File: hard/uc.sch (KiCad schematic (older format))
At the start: 31 parts, among them J3 Conn_01x06, M97 2N7002,215

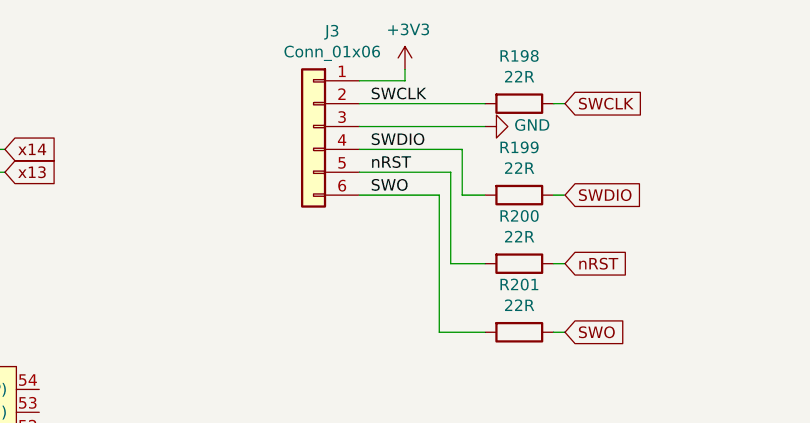
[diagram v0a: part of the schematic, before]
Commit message: added led driver layout by @lukekaese
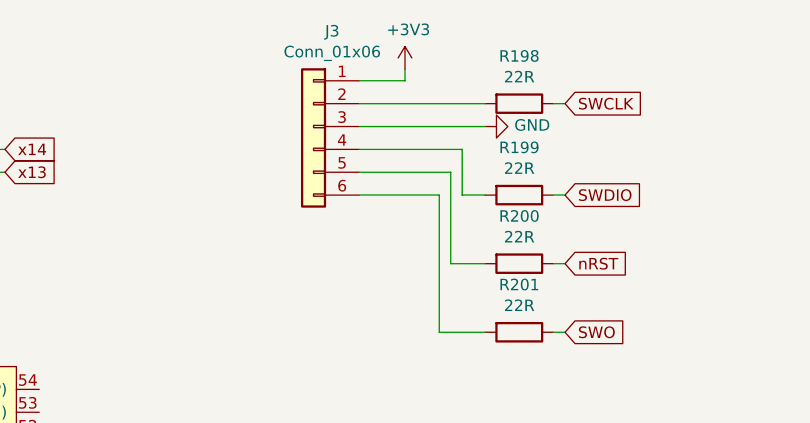
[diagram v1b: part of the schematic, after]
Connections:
- net SWCLK: no longer J3.2 (Pin_2), R198.2
- net SWDIO: no longer J3.4 (Pin_4), R199.2
- net SWO: no longer J3.6 (Pin_6), R201.2
- net nRST: no longer J3.5 (Pin_5), R200.2
- new net: J3.5 (Pin_5), R200.2
- new net: J3.4 (Pin_4), R199.2
- new net: J3.2 (Pin_2), R198.2
- new net: J3.6 (Pin_6), R201.2
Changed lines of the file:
@@
 Text GLabel 9950 5700 2    50   Input ~ 0
 y13
-Text Label 13100 1900 0    50   ~ 0
-SWCLK
-Text Label 13100 2100 0    50   ~ 0
-SWDIO
-Text Label 13100 2200 0    50   ~ 0
-nRST
-Text Label 13100 2300 0    50   ~ 0
-SWO
 Wire Wire Line
 	13050 1900 13600 1900

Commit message: pcb format refactor
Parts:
- J1: renamed from J3; footprint Connector_PinHeader_2.54mm:PinHeader_1x06_P2.54mm_Horizontal -> Connector_PinHeader_2.54mm:PinHeader_1x06_P2.54mm_Vertical
- renumbered C26 to C12, C27 to C13, C12 to C14, C13 to C15, C14 to C16, C5 to C2, C2 to C3, C3 to C4, C4 to C5, D1028 to D1, M97 to M1, R198 to R1, R207 to R10, R199 to R2, R200 to R3, R201 to R4, R204 to R5, R205 to R6, R202 to R7, R203 to R8, R206 to R9

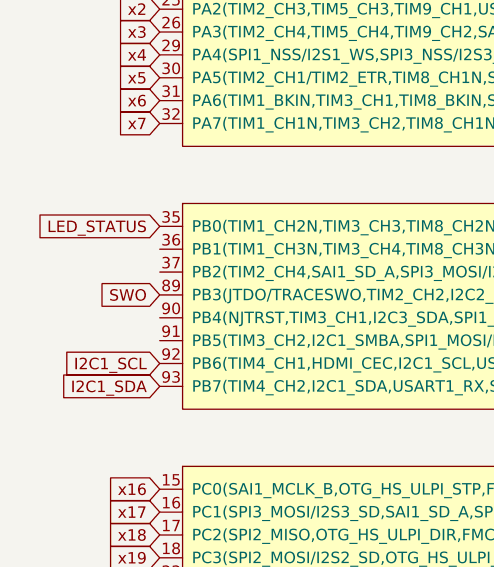
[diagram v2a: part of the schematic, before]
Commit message: general layout update
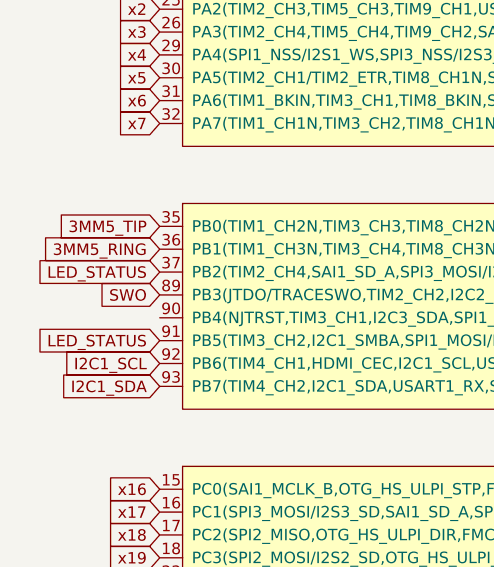
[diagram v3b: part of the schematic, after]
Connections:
- net LED_STATUS: now also MCU1.37 (PB2(TIM2_CH4,SAI1_SD_A,SPI3_MOSI/I2S3_SD,QUADSPI_CLK,OTG_HS_ULPI_D4,SDIO_CK,BOOT1)), MCU1.91 (PB5(TIM3_CH2,I2C1_SMBA,SPI1_MOSI/I2S1_SD,SPI3_MOSI/I2S3_SD,CAN2_RX,OTG_HS_ULPI_D7,FMC_SDCKE1,DCMI_D10)); no longer MCU1.35 (PB0(TIM1_CH2N,TIM3_CH3,TIM8_CH2N,SPI3_MOSI/I2S3_SD,UART4_CTS,OTG_HS_ULPI_D1,SDIO_D1,ADC12_IN8))
- net 3MM5_RING: now reaches MCU1.36 (PB1(TIM1_CH3N,TIM3_CH4,TIM8_CH3N,OTG_HS_ULPI_D2,SDIO_D2,ADC12_IN9))
- new net 3MM5_TIP: MCU1.35 (PB0(TIM1_CH2N,TIM3_CH3,TIM8_CH2N,SPI3_MOSI/I2S3_SD,UART4_CTS,OTG_HS_ULPI_D1,SDIO_D1,ADC12_IN8))
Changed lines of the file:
@@
 Wire Wire Line
 	15950 7500 15950 7550
-Text GLabel 3550 3150 0    50   Input ~ 0
+Text GLabel 3550 3350 0    50   Input ~ 0
 LED_STATUS
 Wire Wire Line
@@
 Wire Wire Line
 	15350 5000 15400 5000
+Text GLabel 3550 3150 0    50   Input ~ 0
+3MM5_TIP
+Text GLabel 3550 3250 0    50   Input ~ 0
+3MM5_RING
+Text GLabel 3550 3650 0    50   Input ~ 0
+LED_STATUS
 $EndSCHEMATC

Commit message: layout process
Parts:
- removed unit 6 of MCU1
- removed R5, R6: 3K3, Resistor_SMD:R_0402_1005Metric, symbol Device:R
- J1: footprint Connector_PinHeader_2.54mm:PinHeader_1x06_P2.54mm_Vertical -> Connector_PinHeader_2.54mm:PinHeader_1x06_P2.54mm_Horizontal
- MCU1: footprint (none) -> Package_QFP:LQFP-100_14x14mm_P0.5mm
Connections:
- net y16: no longer MCU1.97 (PE0(TIM4_ETR,SAI2_MCLK_A,FMC_NBL0,DCMI_D2))
- net y17: no longer MCU1.98 (PE1(FMC_NBL1,DCMI_D3))
- net SPI2_CS_ACC: now reaches MCU1.51 (PB12(TIM1_BKIN,I2C2_SMBA,SPI2_NSS/I2S2_WS,SAI1_SCK_B,USART3_CK,CAN2_RX,OTG_HS_ULPI_D5,OTG_HS_ID))
- net SPI2_SCLK: now reaches MCU1.52 (PB13(TIM1_CH1N,SPI2_SCK/I2S2_CK,USART3_CTS,CAN2_TX,OTG_HS_ULPI_D6,OTG_HS_VBUS))
- net SPI2_MISO: now reaches MCU1.53 (PB14(TIM1_CH2N,TIM8_CH2N,SPI2_MISO,USART3_RTS,TIM12_CH1,OTG_HS_DM))
- net SPI2_MOSI: now reaches MCU1.54 (PB15(RTC_REFIN,TIM1_CH3N,TIM8_CH3N,SPI2_MOSI/I2S2_SD,TIM12_CH2,OTG_HS_DP))
- net SWCLK renamed x14
- net SWDIO renamed x13
- new net ACC_INT1: MCU1.97 (PE0(TIM4_ETR,SAI2_MCLK_A,FMC_NBL0,DCMI_D2))
- new net ACC_INT2: MCU1.98 (PE1(FMC_NBL1,DCMI_D3))
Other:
- note added: "+3V3"
- note added: "GND"
- note added: "SWCLK"
- note added: "SWDIO"
- note added: "SWO"
- note added: "nRST"
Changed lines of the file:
@@
 F 0 "MCU1" H 7300 2065 50  0000 C CNN
 F 1 "STM32F446VE" H 7300 1974 50  0000 C CNN
-F 2 "" H 7850 2250 50  0001 C CNN
+F 2 "Package_QFP:LQFP-100_14x14mm_P0.5mm" H 7850 2250 50  0001 C CNN
 F 3 "https://www.st.com/resource/en/datasheet/stm32f446ve.pdf" H 7850 2250 50  0001 C CNN
 F 4 "C91929" H 7300 1900 50  0001 C CNN "JLCPCB_Part_Number"
@@
 F 0 "MCU1" H 7600 3215 50  0000 C CNN
 F 1 "STM32F446VE" H 7600 3124 50  0000 C CNN
-F 2 "" H 8150 3400 50  0001 C CNN
+F 2 "Package_QFP:LQFP-100_14x14mm_P0.5mm" H 8150 3400 50  0001 C CNN
 F 3 "https://www.st.com/resource/en/datasheet/stm32f446ve.pdf" H 8150 3400 50  0001 C CNN
 F 4 "C91929" H 7600 3050 50  0001 C CNN "JLCPCB_Part_Number"
@@
 F 0 "MCU1" H 7700 4365 50  0000 C CNN
 F 1 "STM32F446VE" H 7700 4274 50  0000 C CNN
-F 2 "" H 8250 4550 50  0001 C CNN
+F 2 "Package_QFP:LQFP-100_14x14mm_P0.5mm" H 8250 4550 50  0001 C CNN
 F 3 "https://www.st.com/resource/en/datasheet/stm32f446ve.pdf" H 8250 4550 50  0001 C CNN
 F 4 "C91929" H 7700 4200 50  0001 C CNN "JLCPCB_Part_Number"
@@
 $Comp
 L led_matrix:STM32F446VE MCU1
-U 6 1 605B418A
-P 4250 7800
-F 0 "MCU1" H 4250 7965 50  0000 C CNN
-F 1 "STM32F446VE" H 4250 7874 50  0000 C CNN
-F 2 "" H 4800 8150 50  0001 C CNN
-F 3 "https://www.st.com/resource/en/datasheet/stm32f446ve.pdf" H 4800 8150 50  0001 C CNN
-F 4 "C91929" H 4250 7800 50  0001 C CNN "JLCPCB_Part_Number"
-F 5 "STMicroelectronics" H 4250 7800 50  0001 C CNN "MF"
-F 6 "STM32F446VET6" H 4250 7800 50  0001 C CNN "MPN"
-F 7 "ST MICROELECTRONICS LQFP-100_14X14X05P ROHS" H 4250 7800 50  0001 C CNN "Description"
-	6    4250 7800
-	1    0    0    -1
-$EndComp
-$Comp
-L led_matrix:STM32F446VE MCU1
 U 7 1 605B81AB
 P 12900 6100
 F 0 "MCU1" H 12900 6265 50  0000 C CNN
 F 1 "STM32F446VE" H 12900 6174 50  0000 C CNN
-F 2 "" H 13450 6450 50  0001 C CNN
+F 2 "Package_QFP:LQFP-100_14x14mm_P0.5mm" H 13450 6450 50  0001 C CNN
 F 3 "https://www.st.com/resource/en/datasheet/stm32f446ve.pdf" H 13450 6450 50  0001 C CNN
 F 4 "C91929" H 12900 6100 50  0001 C CNN "JLCPCB_Part_Number"
@@
 	11200 6200 11250 6200
 Text GLabel 13950 1900 2    50   Input ~ 0
-SWCLK
+x14
 Text GLabel 13950 2300 2    50   Input ~ 0
-SWDIO
+x13
 $Comp
 L power:GND #PWR02
@@
 L power:+3V3 #PWR01
 U 1 1 6266BC9A
-P 13250 1750
-F 0 "#PWR01" H 13250 1600 50  0001 C CNN
-F 1 "+3V3" H 13265 1923 50  0000 C CNN
-F 2 "" H 13250 1750 50  0001 C CNN
-F 3 "" H 13250 1750 50  0001 C CNN
-	1    13250 1750
+P 13600 1750
+F 0 "#PWR01" H 13600 1600 50  0001 C CNN
+F 1 "+3V3" H 13615 1923 50  0000 C CNN
+F 2 "" H 13600 1750 50  0001 C CNN
+F 3 "" H 13600 1750 50  0001 C CNN
+	1    13600 1750
 	1    0    0    -1
 $EndComp
@@
 F 0 "J1" H 12768 2417 50  0000 C CNN
 F 1 "Conn_01x06" H 12768 2326 50  0000 C CNN
-F 2 "Connector_PinHeader_2.54mm:PinHeader_1x06_P2.54mm_Vertical" H 12850 2000 50  0001 C CNN
+F 2 "Connector_PinHeader_2.54mm:PinHeader_1x06_P2.54mm_Horizontal" H 12850 2000 50  0001 C CNN
 F 3 "~" H 12850 2000 50  0001 C CNN
 	1    12850 2000
@@
 SWO
 Wire Wire Line
-	13050 1800 13250 1800
-Wire Wire Line
-	13250 1800 13250 1750
+	13050 1800 13600 1800
+Wire Wire Line
+	13600 1800 13600 1750
 Wire Wire Line
 	13900 2900 13950 2900
@@
 Text GLabel 3550 3850 0    50   Input ~ 0
 I2C1_SDA
-$Comp
-L Device:R R5
-U 1 1 627218B8
-P 15350 5200
-F 0 "R5" H 15281 5154 50  0000 R CNN
-F 1 "3K3" H 15281 5245 50  0000 R CNN
-F 2 "Resistor_SMD:R_0402_1005Metric" V 15280 5200 50  0001 C CNN
-F 3 "~" H 15350 5200 50  0001 C CNN
-	1    15350 5200
-	1    0    0    1
-$EndComp
-$Comp
-L Device:R R6
-U 1 1 62734FB0
-P 15450 5200
-F 0 "R6" H 15380 5154 50  0000 R CNN
-F 1 "3K3" H 15380 5245 50  0000 R CNN
-F 2 "Resistor_SMD:R_0402_1005Metric" V 15380 5200 50  0001 C CNN
-F 3 "~" H 15450 5200 50  0001 C CNN
-	1    15450 5200
-	-1   0    0    1
-$EndComp
-$Comp
-L power:+3V3 #PWR03
-U 1 1 62752189
-P 15400 4950
-F 0 "#PWR03" H 15400 4800 50  0001 C CNN
-F 1 "+3V3" H 15415 5123 50  0000 C CNN
-F 2 "" H 15400 4950 50  0001 C CNN
-F 3 "" H 15400 4950 50  0001 C CNN
-	1    15400 4950
-	1    0    0    -1
-$EndComp
-Text GLabel 15350 5400 3    50   Input ~ 0
-I2C1_SDA
-Text GLabel 15450 5400 3    50   Input ~ 0
-I2C1_SCL
-Wire Wire Line
-	15350 5050 15350 5000
-Wire Wire Line
-	15450 5000 15450 5050
-Wire Wire Line
-	15400 5000 15400 4950
-Connection ~ 15400 5000
-Text Notes 16900 3950 0    50   ~ 0
+Text Notes 12300 4150 0    50   ~ 0
 todo: recheck pins\n
 Text GLabel 3550 2000 0    50   Input ~ 0
@@
 Text GLabel 11050 2300 2    50   Input ~ 0
 x12
-Text GLabel 11500 2200 2    50   Input ~ 0
+Text GLabel 11050 2200 2    50   Input ~ 0
 x13
-Text GLabel 11500 2100 2    50   Input ~ 0
+Text GLabel 11050 2100 2    50   Input ~ 0
 x14
 Text GLabel 11050 2000 2    50   Input ~ 0
@@
 F 0 "MCU1" H 5900 6765 50  0000 C CNN
 F 1 "STM32F446VE" H 5900 6674 50  0000 C CNN
-F 2 "" H 6450 6950 50  0001 C CNN
+F 2 "Package_QFP:LQFP-100_14x14mm_P0.5mm" H 6450 6950 50  0001 C CNN
 F 3 "https://www.st.com/resource/en/datasheet/stm32f446ve.pdf" H 6450 6950 50  0001 C CNN
 F 4 "C91929" H 5900 6600 50  0001 C CNN "JLCPCB_Part_Number"
@@
 Wire Wire Line
 	13050 2300 13400 2300
-Text GLabel 3550 6700 0    50   Input ~ 0
+Text GLabel 2950 6700 0    50   Input ~ 0
 y16
-Text GLabel 3550 6800 0    50   Input ~ 0
+Text GLabel 2950 6800 0    50   Input ~ 0
 y17
 Text GLabel 3550 6900 0    50   Input ~ 0
 y18
-Wire Wire Line
-	11050 2100 11500 2100
-Wire Wire Line
-	11500 2200 11050 2200
-Text GLabel 11400 2100 1    50   Input ~ 0
-SWCLK
-Text GLabel 11400 2200 3    50   Input ~ 0
-SWDIO
 Text GLabel 3550 3450 0    50   Input ~ 0
 SWO
@@
 Text GLabel 3550 5500 0    50   Input ~ 0
 y0
-Wire Wire Line
-	15350 5400 15350 5350
-Wire Wire Line
-	15450 5400 15450 5350
-Wire Wire Line
-	15400 5000 15450 5000
-Wire Wire Line
-	15350 5000 15400 5000
 Text GLabel 3550 3150 0    50   Input ~ 0
 3MM5_TIP
@@
 Text GLabel 3550 3650 0    50   Input ~ 0
 LED_STATUS
+Text GLabel 11650 3150 2    50   Input ~ 0
+SPI2_MOSI
+Text GLabel 11650 3250 2    50   Input ~ 0
+SPI2_MISO
+Text GLabel 11650 3350 2    50   Input ~ 0
+SPI2_SCLK
+Text GLabel 11650 3450 2    50   Input ~ 0
+SPI2_CS_ACC
+Text Notes 12800 1800 2    50   ~ 0
++3V3
+Text Notes 12800 1900 2    50   ~ 0
+SWCLK
+Text Notes 12800 2000 2    50   ~ 0
+GND
+Text Notes 12800 2100 2    50   ~ 0
+SWDIO
+Text Notes 12800 2200 2    50   ~ 0
+nRST
+Text Notes 12800 2300 2    50   ~ 0
+SWO
+Text GLabel 3550 6700 0    50   Input ~ 0
+ACC_INT1
+Text GLabel 3550 6800 0    50   Input ~ 0
+ACC_INT2
 $EndSCHEMATC

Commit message: layout progress. todo: led drivers
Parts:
- MCU1: footprint Package_QFP:LQFP-100_14x14mm_P0.5mm -> led_matrix:LQFP-100_14x14mm_P0.5mm; DigiKey_Part_Number (none) -> 497-15375-ND
- MCU1: footprint Package_QFP:LQFP-100_14x14mm_P0.5mm -> led_matrix:LQFP-100_14x14mm_P0.5mm
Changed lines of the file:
@@
 F 0 "MCU1" H 7300 2065 50  0000 C CNN
 F 1 "STM32F446VE" H 7300 1974 50  0000 C CNN
-F 2 "Package_QFP:LQFP-100_14x14mm_P0.5mm" H 7850 2250 50  0001 C CNN
+F 2 "led_matrix:LQFP-100_14x14mm_P0.5mm" H 7850 2250 50  0001 C CNN
 F 3 "https://www.st.com/resource/en/datasheet/stm32f446ve.pdf" H 7850 2250 50  0001 C CNN
 F 4 "C91929" H 7300 1900 50  0001 C CNN "JLCPCB_Part_Number"
@@
 F 6 "STM32F446VET6" H 7300 1900 50  0001 C CNN "MPN"
 F 7 "ST MICROELECTRONICS LQFP-100_14X14X05P ROHS" H 7300 1900 50  0001 C CNN "Description"
+F 8 "497-15375-ND" H 7300 1900 50  0001 C CNN "DigiKey_Part_Number"
 	1    7300 1900
 	1    0    0    -1
@@
 F 0 "MCU1" H 7600 3215 50  0000 C CNN
 F 1 "STM32F446VE" H 7600 3124 50  0000 C CNN
-F 2 "Package_QFP:LQFP-100_14x14mm_P0.5mm" H 8150 3400 50  0001 C CNN
+F 2 "led_matrix:LQFP-100_14x14mm_P0.5mm" H 8150 3400 50  0001 C CNN
 F 3 "https://www.st.com/resource/en/datasheet/stm32f446ve.pdf" H 8150 3400 50  0001 C CNN
 F 4 "C91929" H 7600 3050 50  0001 C CNN "JLCPCB_Part_Number"
@@
 F 0 "MCU1" H 7700 4365 50  0000 C CNN
 F 1 "STM32F446VE" H 7700 4274 50  0000 C CNN
-F 2 "Package_QFP:LQFP-100_14x14mm_P0.5mm" H 8250 4550 50  0001 C CNN
+F 2 "led_matrix:LQFP-100_14x14mm_P0.5mm" H 8250 4550 50  0001 C CNN
 F 3 "https://www.st.com/resource/en/datasheet/stm32f446ve.pdf" H 8250 4550 50  0001 C CNN
 F 4 "C91929" H 7700 4200 50  0001 C CNN "JLCPCB_Part_Number"
@@
 F 0 "MCU1" H 6750 5565 50  0000 C CNN
 F 1 "STM32F446VE" H 6750 5474 50  0000 C CNN
-F 2 "Package_QFP:LQFP-100_14x14mm_P0.5mm" H 7300 5750 50  0001 C CNN
+F 2 "led_matrix:LQFP-100_14x14mm_P0.5mm" H 7300 5750 50  0001 C CNN
 F 3 "https://www.st.com/resource/en/datasheet/stm32f446ve.pdf" H 7300 5750 50  0001 C CNN
 F 4 "C91929" H 6750 5400 50  0001 C CNN "JLCPCB_Part_Number"
@@
 F 0 "MCU1" H 12900 6265 50  0000 C CNN
 F 1 "STM32F446VE" H 12900 6174 50  0000 C CNN
-F 2 "Package_QFP:LQFP-100_14x14mm_P0.5mm" H 13450 6450 50  0001 C CNN
+F 2 "led_matrix:LQFP-100_14x14mm_P0.5mm" H 13450 6450 50  0001 C CNN
 F 3 "https://www.st.com/resource/en/datasheet/stm32f446ve.pdf" H 13450 6450 50  0001 C CNN
 F 4 "C91929" H 12900 6100 50  0001 C CNN "JLCPCB_Part_Number"
@@
 F 0 "MCU1" H 5900 6765 50  0000 C CNN
 F 1 "STM32F446VE" H 5900 6674 50  0000 C CNN
-F 2 "Package_QFP:LQFP-100_14x14mm_P0.5mm" H 6450 6950 50  0001 C CNN
+F 2 "led_matrix:LQFP-100_14x14mm_P0.5mm" H 6450 6950 50  0001 C CNN
 F 3 "https://www.st.com/resource/en/datasheet/stm32f446ve.pdf" H 6450 6950 50  0001 C CNN
 F 4 "C91929" H 5900 6600 50  0001 C CNN "JLCPCB_Part_Number"
